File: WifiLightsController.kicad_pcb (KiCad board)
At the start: 2 copper layers, 49.8 x 22 mm, 10 parts, among them P1 CONN_01X04, P2 CONN_01X04, P3 CONN_01X03, P4 CONN_01X02, SW1 SW_PUSH, SW2 PASSIVES_Switch_DPDT, U1 LD1117S33CTR

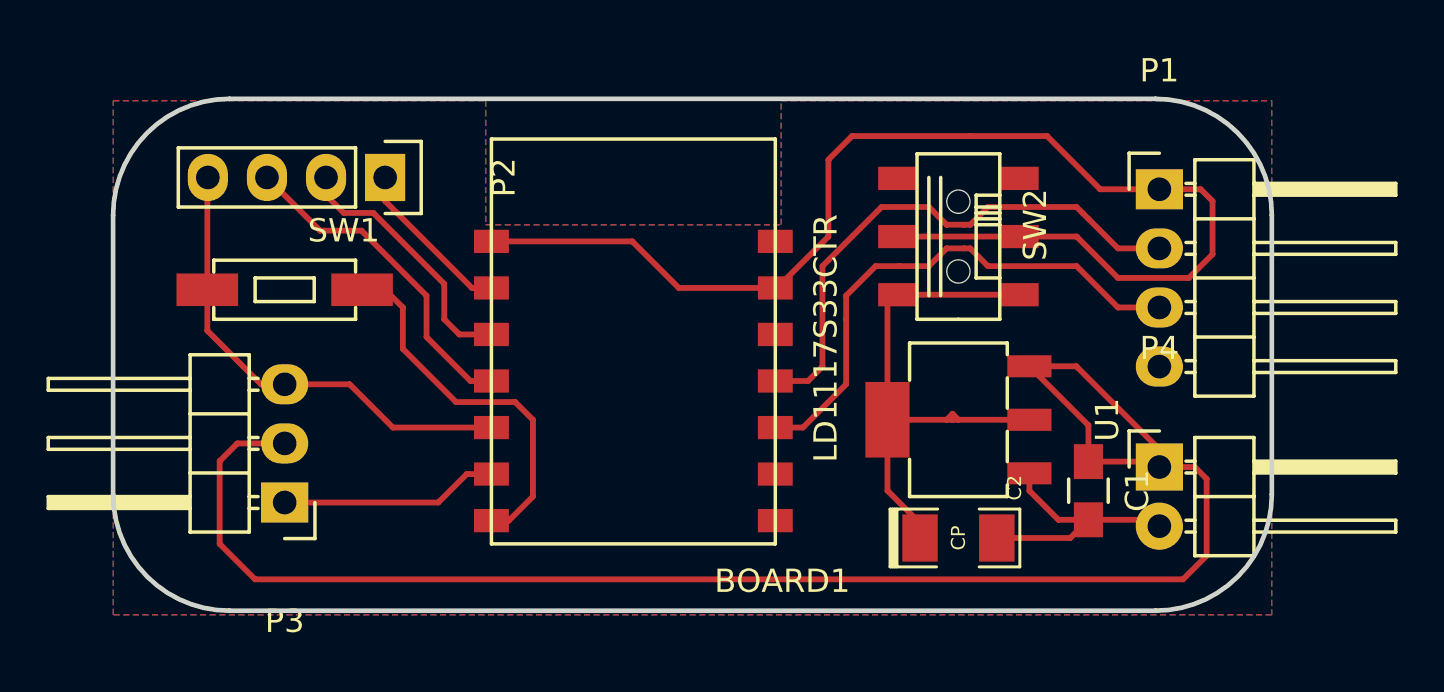
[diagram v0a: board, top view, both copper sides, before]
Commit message: Routed board. Add silkcreen ids
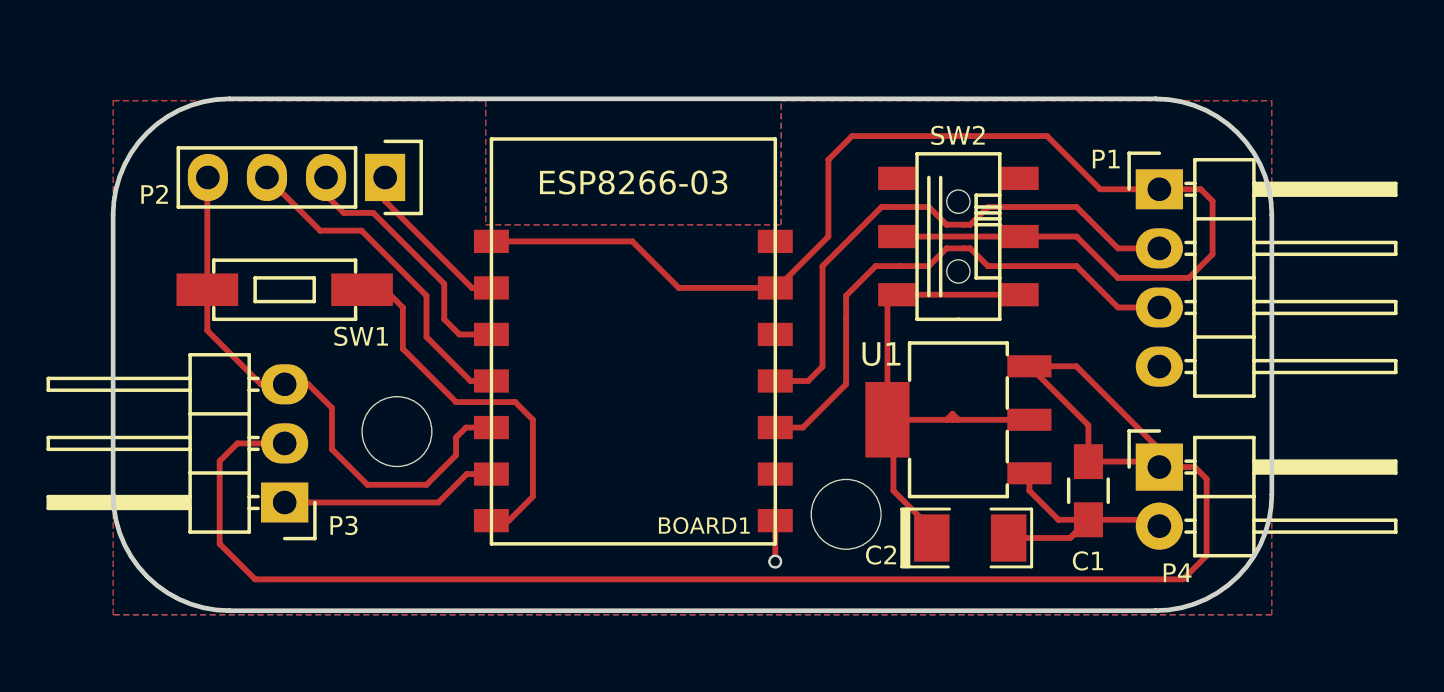
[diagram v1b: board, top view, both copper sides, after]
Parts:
- added Mechanical_drill_3mm: , def-footprints:Mechanical_Drill_3mm, F.Cu at (149.9, 82.3)
- added Mechanical_drill_3mm: , def-footprints:Mechanical_Drill_3mm, F.Cu at (169.2, 85.9)
- moved C2 0.51 mm to (174.5, 86.9)
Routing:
- net GND: track 33.1 -> 39.0 mm, vias 0 -> 1
- net Net-(C2-Pad1): track 23.8 -> 24.6 mm

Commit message: First prototype
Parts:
- added G***: OSHW-logo, def-footprints:Logo_OSHW_small, F.Cu at (160.0, 79.5)
- added G***: LOGO, def-footprints:Logo_OSHW_3x3cm, B.Cu at (164.6, 68.1)
- moved Mechanical_drill_3mm 0.30 mm to (149.7, 82.1)
- moved Mechanical_drill_3mm 0.29 mm to (169.5, 85.9)
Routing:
- added copper zone on F.Cu, net +5V
- added copper zone on F.Cu, net GND
- added copper zone on F.Cu, net Net-(C2-Pad1)
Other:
- board text added: "+5V"
- board text added: "3V3"
- board text added: "David Estevez Fdez"
- board text added: "GND"
- board text added: "GPIO12"
- board text added: "GPIO13"
- board text added: "GPIO14"
- board text added: "GPIO2"
- board text added: "RX"
- board text added: "TX"
- board text added: "WifiLightsController"
- board text added: "v1.0"
